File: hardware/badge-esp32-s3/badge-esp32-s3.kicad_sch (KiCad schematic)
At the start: 9 parts, among them U1 ESP32-S3-MINI-1-N4R2

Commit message: final changes and part updated
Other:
- sheet GPIO Header Block ports: added IO10, IO11, IO12, IO21, IO33, IO34, IO47, IO48, IO8, IO9; removed IO1, IO14, IO15, IO16, IO17, IO18, IO38, IO41, IO42, IO43
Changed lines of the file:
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@@
 	(wire
 		(pts
+			(xy 223.52 133.35) (xy 224.79 133.35)
+		)
+		(stroke
+			(width 0)
+			(type default)
+		)
+	)
+	(wire
+		(pts
 			(xy 251.46 148.59) (xy 255.27 148.59)
 		)
@@
 	(wire
 		(pts
+			(xy 223.52 130.81) (xy 224.79 130.81)
+		)
+		(stroke
+			(width 0)
+			(type default)
+		)
+	)
+	(wire
+		(pts
 			(xy 251.46 106.68) (xy 255.27 106.68)
 		)
@@
 	(wire
 		(pts
-			(xy 224.79 133.35) (xy 223.52 133.35)
-		)
-		(stroke
-			(width 0)
-			(type default)
-		)
-	)
-	(wire
-		(pts
 			(xy 73.66 48.26) (xy 73.66 45.72)
 		)
@@
 	(wire
 		(pts
-			(xy 224.79 130.81) (xy 223.52 130.81)
-		)
-		(stroke
-			(width 0)
-			(type default)
-		)
-	)
-	(wire
-		(pts
 			(xy 195.58 107.95) (xy 196.85 107.95)
 		)
@@
 	)
 	(label "AddrLedMid"
-		(at 224.79 110.49 0)
+		(at 224.79 115.57 0)
 		(effects
 			(font
@@
 	)
 	(label "JoystickXMid"
-		(at 224.79 105.41 0)
+		(at 224.79 118.11 0)
 		(effects
 			(font
@@
 	)
 	(label "DownButtonMid"
-		(at 224.79 118.11 0)
+		(at 224.79 130.81 0)
 		(effects
 			(font
@@
 	)
 	(label "UpButtonMid"
-		(at 224.79 120.65 0)
+		(at 224.79 125.73 0)
 		(effects
 			(font
@@
 	)
 	(label "LeftButtonMid"
-		(at 224.79 115.57 0)
+		(at 224.79 128.27 0)
 		(effects
 			(font
@@
 	)
 	(label "AButtonMid"
-		(at 224.79 125.73 0)
+		(at 224.79 135.89 0)
 		(effects
 			(font
@@
 	)
 	(label "BButtonMid"
-		(at 224.79 123.19 0)
+		(at 224.79 133.35 0)
 		(effects
 			(font
@@
 	)
 	(label "RightButtonMid"
-		(at 224.79 113.03 0)
+		(at 224.79 123.19 0)
 		(effects
 			(font
@@
 	)
 	(label "JoystickYMid"
-		(at 224.79 107.95 0)
+		(at 224.79 120.65 0)
 		(effects
 			(font
@@
 	)
 	(label "LEDSingleMid"
-		(at 224.79 135.89 0)
+		(at 224.79 113.03 0)
 		(effects
 			(font
@@
 	)
 	(label "RGBGreenMid"
-		(at 224.79 130.81 0)
+		(at 224.79 107.95 0)
 		(effects
 			(font
@@
 	)
 	(label "RGBBlueMid"
-		(at 224.79 133.35 0)
+		(at 224.79 110.49 0)
 		(effects
 			(font
@@
 	)
 	(label "RGBRedMid"
-		(at 224.79 128.27 0)
+		(at 224.79 105.41 0)
 		(effects
 			(font
@@
 			)
 		)
-		(pin "JoystickXMid" input
-			(at 223.52 105.41 0)
+		(pin "IO2" bidirectional
+			(at 196.85 105.41 180)
 			(effects
 				(font
 					(size 1.27 1.27)
 				)
-				(justify right)
+				(justify left)
 			)
 		)
-		(pin "AButtonMid" input
-			(at 223.52 125.73 0)
+		(pin "IO4" bidirectional
+			(at 196.85 107.95 180)
 			(effects
 				(font
 					(size 1.27 1.27)
 				)
-				(justify right)
+				(justify left)
 			)
 		)
-		(pin "BButtonMid" input
-			(at 223.52 123.19 0)
+		(pin "IO5" bidirectional
+			(at 196.85 110.49 180)
 			(effects
 				(font
 					(size 1.27 1.27)
 				)
-				(justify right)
+				(justify left)
 			)
 		)
-		(pin "Buzzer" output
-			(at 223.52 138.43 0)
+		(pin "IO6" bidirectional
+			(at 196.85 113.03 180)
 			(effects
 				(font
 					(size 1.27 1.27)
 				)
-				(justify right)
+				(justify left)
 			)
 		)
-		(pin "DownButtonMid" input
-			(at 223.52 118.11 0)
+		(pin "IO7" bidirectional
+			(at 196.85 115.57 180)
 			(effects
 				(font
 					(size 1.27 1.27)
 				)
-				(justify right)
+				(justify left)
 			)
 		)
-		(pin "IO1" bidirectional
-			(at 196.85 105.41 180)
+		(pin "IO8" bidirectional
+			(at 196.85 118.11 180)
 			(effects
 				(font
@@
 			)
 		)
-		(pin "IO2" bidirectional
-			(at 196.85 107.95 180)
+		(pin "IO9" bidirectional
+			(at 196.85 120.65 180)
 			(effects
 				(font
@@
 			)
 		)
-		(pin "IO14" bidirectional
-			(at 196.85 113.03 180)
+		(pin "IO10" bidirectional
+			(at 196.85 123.19 180)
 			(effects
 				(font
@@
 			)
 		)
-		(pin "IO15" bidirectional
-			(at 196.85 115.57 180)
+		(pin "IO11" bidirectional
+			(at 196.85 125.73 180)
 			(effects
 				(font
@@
 			)
 		)
-		(pin "IO16" bidirectional
-			(at 196.85 118.11 180)
+		(pin "IO12" bidirectional
+			(at 196.85 140.97 180)
 			(effects
 				(font
@@
 			)
 		)
-		(pin "IO17" bidirectional
-			(at 196.85 120.65 180)
+		(pin "IO21" bidirectional
+			(at 196.85 128.27 180)
 			(effects
 				(font
@@
 			)
 		)
-		(pin "IO18" bidirectional
-			(at 196.85 123.19 180)
+		(pin "IO33" bidirectional
+			(at 196.85 133.35 180)
 			(effects
 				(font
@@
 			)
 		)
-		(pin "IO38" bidirectional
-			(at 196.85 125.73 180)
+		(pin "IO34" bidirectional
+			(at 196.85 135.89 180)
 			(effects
 				(font
@@
 			)
 		)
-		(pin "IO4" bidirectional
-			(at 196.85 133.35 180)
+		(pin "IO47" bidirectional
+			(at 196.85 130.81 180)
 			(effects
 				(font
@@
 			)
 		)
-		(pin "IO5" bidirectional
-			(at 196.85 130.81 180)
+		(pin "IO48" bidirectional
+			(at 196.85 138.43 180)
 			(effects
 				(font
@@
 			)
 		)
-		(pin "IO6" bidirectional
-			(at 196.85 128.27 180)
+		(pin "AButtonMid" input
+			(at 223.52 135.89 0)
 			(effects
 				(font
 					(size 1.27 1.27)
 				)
-				(justify left)
+				(justify right)
 			)
 		)
-		(pin "IO41" bidirectional
-			(at 196.85 135.89 180)
+		(pin "AddrLED" input
+			(at 223.52 115.57 0)
 			(effects
 				(font
 					(size 1.27 1.27)
 				)
-				(justify left)
+				(justify right)
 			)
 		)
-		(pin "IO42" bidirectional
-			(at 196.85 138.43 180)
+		(pin "BButtonMid" input
+			(at 223.52 133.35 0)
 			(effects
 				(font
 					(size 1.27 1.27)
 				)
-				(justify left)
+				(justify right)
 			)
 		)
-		(pin "JoystickYMid" input
-			(at 223.52 107.95 0)
+		(pin "Buzzer" output
+			(at 223.52 138.43 0)
 			(effects
 				(font
@@
 			)
 		)
-		(pin "LEDSingle" output
-			(at 223.52 135.89 0)
+		(pin "DownButtonMid" input
+			(at 223.52 130.81 0)
 			(effects
 				(font
@@
 			)
 		)
-		(pin "LeftButtonMid" input
-			(at 223.52 115.57 0)
+		(pin "JoystickXMid" input
+			(at 223.52 118.11 0)
 			(effects
 				(font
@@
 			)
 		)
-		(pin "RGBBlueMid" output
-			(at 223.52 133.35 0)
+		(pin "JoystickYMid" input
+			(at 223.52 120.65 0)
 			(effects
 				(font
@@
 			)
 		)
-		(pin "RGBGreenMid" output
-			(at 223.52 130.81 0)
+		(pin "LEDSingle" output
+			(at 223.52 113.03 0)
 			(effects
 				(font
@@
 			)
 		)
-		(pin "RGBRedMid" output
+		(pin "LeftButtonMid" input
 			(at 223.52 128.27 0)
 			(effects
@@
 			)
 		)
-		(pin "RightButtonMid" input
-			(at 223.52 113.03 0)
+		(pin "RGBBlueMid" output
+			(at 223.52 110.49 0)
 			(effects
 				(font
@@
 			)
 		)
-		(pin "UpButtonMid" input
-			(at 223.52 120.65 0)
+		(pin "RGBGreenMid" output
+			(at 223.52 107.95 0)
 			(effects
 				(font
@@
 			)
 		)
-		(pin "AddrLED" input
-			(at 223.52 110.49 0)
+		(pin "RGBRedMid" output
+			(at 223.52 105.41 0)
 			(effects
 				(font
@@
 			)
 		)
-		(pin "IO7" bidirectional
-			(at 196.85 110.49 180)
+		(pin "RightButtonMid" input
+			(at 223.52 123.19 0)
 			(effects
 				(font
 					(size 1.27 1.27)
 				)
-				(justify left)
+				(justify right)
 			)
 		)
-		(pin "BatteryVoltage" output
-			(at 223.52 140.97 0)
+		(pin "UpButtonMid" input
+			(at 223.52 125.73 0)
 			(effects
 				(font
@@
 			)
 		)
-		(pin "IO43" bidirectional
-			(at 196.85 140.97 180)
+		(pin "BatteryVoltage" input
+			(at 223.52 140.97 0)
 			(effects
 				(font
 					(size 1.27 1.27)
 				)
-				(justify left)
+				(justify right)
 			)
 		)

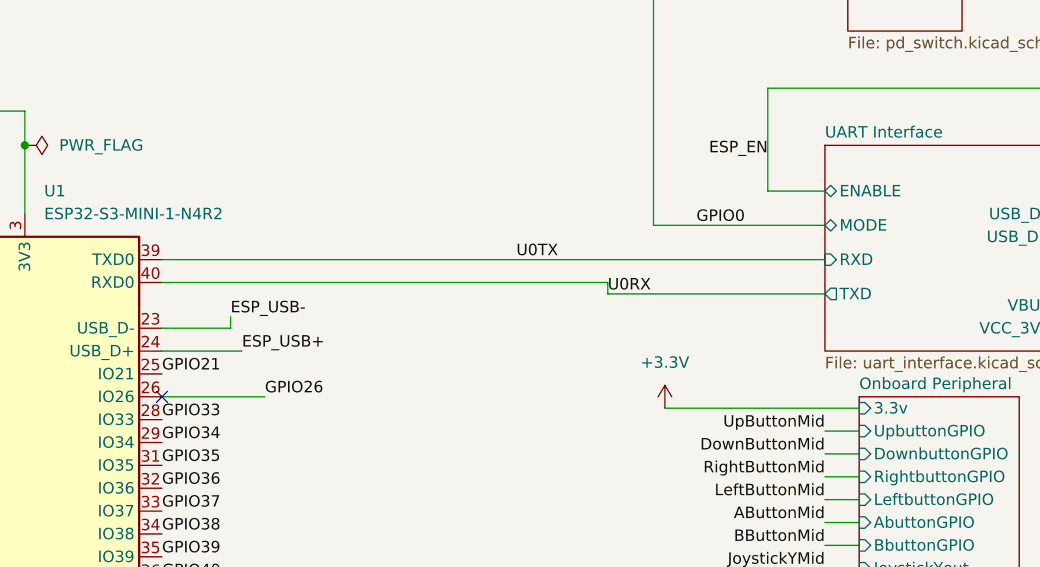
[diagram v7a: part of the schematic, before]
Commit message: finished component alignment
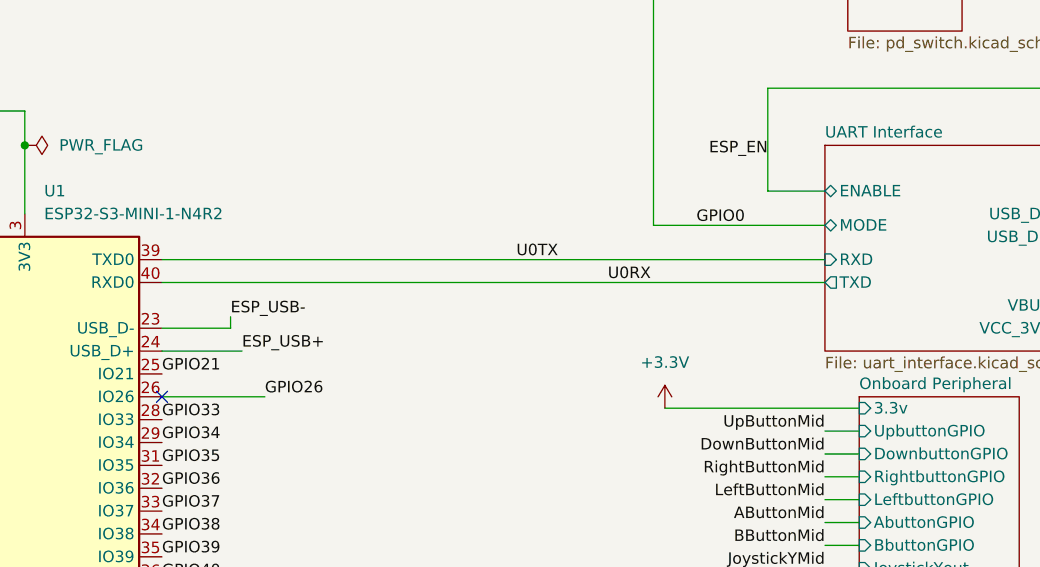
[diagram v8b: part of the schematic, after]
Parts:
- U1: FT Position Offset (none) -> 0,-2.4765
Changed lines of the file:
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@@
 	(wire
 		(pts
-			(xy 182.88 54.61) (xy 182.88 55.88)
-		)
-		(stroke
-			(width 0)
-			(type default)
-		)
-	)
-	(wire
-		(pts
 			(xy 195.58 125.73) (xy 196.85 125.73)
 		)
@@
 	(wire
 		(pts
-			(xy 133.35 54.61) (xy 182.88 54.61)
-		)
-		(stroke
-			(width 0)
-			(type default)
-		)
-	)
-	(wire
-		(pts
 			(xy 223.52 130.81) (xy 224.79 130.81)
 		)
@@
 	(wire
 		(pts
-			(xy 182.88 55.88) (xy 207.01 55.88)
+			(xy 133.35 54.61) (xy 207.01 54.61)
 		)
 		(stroke
@@
 	)
 	(label "U0RX"
-		(at 182.88 55.88 0)
+		(at 182.88 54.61 0)
 		(effects
 			(font
@@
 			)
 		)
+		(property "FT Position Offset" "0,-2.4765"
+			(at 118.11 77.47 0)
+			(effects
+				(font
+					(size 1.27 1.27)
+				)
+				(hide yes)
+			)
+		)
 		(pin "55"
 		)
@@
 		)
 		(pin "TXD" output
-			(at 207.01 55.88 180)
+			(at 207.01 54.61 180)
 			(effects
 				(font
